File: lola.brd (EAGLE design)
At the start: 100 x 80 mm, 1 part, among them U1 ATMEGA328P_TQFP

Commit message: Base modules
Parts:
- added C1, C11, C14, C2, C3, C4, C7, C8, C9: 0.1uF, resistor:C0603
- added C10, C12, C13: 4.7uF, resistor:C0603
- added C5, C6: 22pF, resistor:C0603
- added CN1: (no value), adafruit:USB-MINIB
- added D1, D2: transil, SparkFun-DiscreteSemi:SOD-323
- added D3: (no value), SparkFun-DiscreteSemi:SMA-DIODE
- added F1, F3: 6V/0.5A, SparkFun-Fuses:1206
- added F2: (no value), adafruit:1812
- added IC1: FT232RL, ftdichip:SSOP28
- added IC2: MCP73833-UN, adafruit:MSOP10
- added L1: LQH32PN4R7NN0L, rcl:L1812
- added LED1, LED2: (no value), adafruit:CHIPLED_0805
- added Q1: (no value), SparkFun-DiscreteSemi:SOT23-3
- added R1, R5, R6, R9: 10K, resistor:R0603
- added R2: 1M, resistor:R0603
- added R3, R4: 1K, resistor:R0603
- added R7: 2K, resistor:R0603
- added R8: 10K ntc, resistor:R0603
- added U$1: MCP1603T-330I/OS, MCP1603T-330I_OS:SOT95P280X110-5N
- added U$2, U$3: COMF_BHC-18650-1P, FloManEagle:MR18650_HOLDER
- added U2: RFM69HW, SparkFun-RF:RFM69W-XXXS2
- added U3: AT24C256C-SSHL-T, AT24C256C-SSHL-T:SOIC127P600X175-8N
- added U4: ADS1115IDGST, ADS1115IDGST:SOP50P490X110-10N
- added X1: (no value), adafruit:SMA_EDGELAUNCH_UFL
- added Y1: 8MHz, SparkFun-Clocks:CRYSTAL-SMD-5X3.2-4PAD
- moved U1 59.9 mm to (10.7, 60.3), turned to 180 degrees
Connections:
- new net !EXT_RESET: C8.2, IC1.3
- new net !RESET: C8.1, R1.2, U1.29
- new net 3.3V: C1.1, C10.1, C11.1, C14.1, C2.1, C3.1, C4.1, C9.1, F3.2, R1.1, R5.2, R6.2, U1.18, U1.20, U1.4, U1.6, U2.8, U3.8, U4.8
- new net 5V: D3.A, F1.2, IC1.20, IC2.1, IC2.2, Q1.1, R9.2
- new net ADC_RDY: U4.2
- new net AIN0: U4.4
- new net AIN1: U4.5
- new net AIN2: U4.6
- new net AIN3: U4.7
- new net CHG: IC2.3
- new net FT_3.3V: C7.1, IC1.17, IC1.4, R3.2, R4.2
- new net FULL: IC2.4
- new net GND: C1.2, C10.2, C11.2, C12.2, C13.2, C14.2, C2.2, C3.2, C4.2, C5.2, C6.2, C7.2, C9.2, CN1.GND, D1.A, D2.A, IC1.18, IC1.21, IC1.25, IC1.7, IC2.5, R7.2, R8.2, R9.1, U$1.2, U$2.P$2, U$3.P$2, U1.21, U1.3, U1.5, U2.11, U2.9, U3.1, U3.2, U3.3, U3.4, U3.7, U4.1, U4.3, X1.GND@1, X1.GND@2, X1.GND@3, X1.GND@4, Y1.2, Y1.4
- new net MISO: U1.16, U2.13
- new net MOSI: U1.15, U2.14
- new net N$1: U2.10, X1.P
- new net N$10: U1.2
- new net N$11: U1.9
- new net N$12: U1.10
- new net N$13: U1.11
- new net N$14: U1.12
- new net N$15: U1.13
- new net N$16: U1.14
- new net N$17: C5.1, R2.2, U1.7, Y1.3
- new net N$18: C6.1, R2.1, U1.8, Y1.1
- new net N$19: IC2.8, R8.1
- new net N$2: F2.1, U$2.P$1
- new net N$20: CN1.VBUS, F1.1
- new net N$21: CN1.D+, D2.C, IC1.15
- new net N$22: CN1.D-, D1.C, IC1.16
- new net N$23: LED2.A, R4.1
- new net N$24: IC1.22, LED2.C
- new net N$25: IC1.23, LED1.C
- new net N$26: LED1.A, R3.1
- new net N$28: IC2.6, R7.1
- new net N$29: L1.2, U$1.5
- new net N$3: C13.1, F3.1, L1.1, U$1.4
- new net N$4: U1.23
- new net N$5: U1.24
- new net N$6: U1.25
- new net N$7: U1.26
- new net N$8: U1.32
- new net N$9: U1.1
- new net RF_INT: U2.2
- new net RF_SS: U2.15
- new net RX: IC1.1, U1.30
- new net SCK: U1.17, U2.12
- new net SCL: R5.1, U1.28, U3.6, U4.10
- new net SDA: R6.1, U1.27, U3.5, U4.9
- new net TX: IC1.5, U1.31
- new net VCC: D3.C, Q1.2, U$1.1, U$1.3
- new net V_BATT: C12.1, F2.2, IC2.10, IC2.9, Q1.3, U$3.P$1
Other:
- board size 100 x 80 mm -> 45 x 100 mm

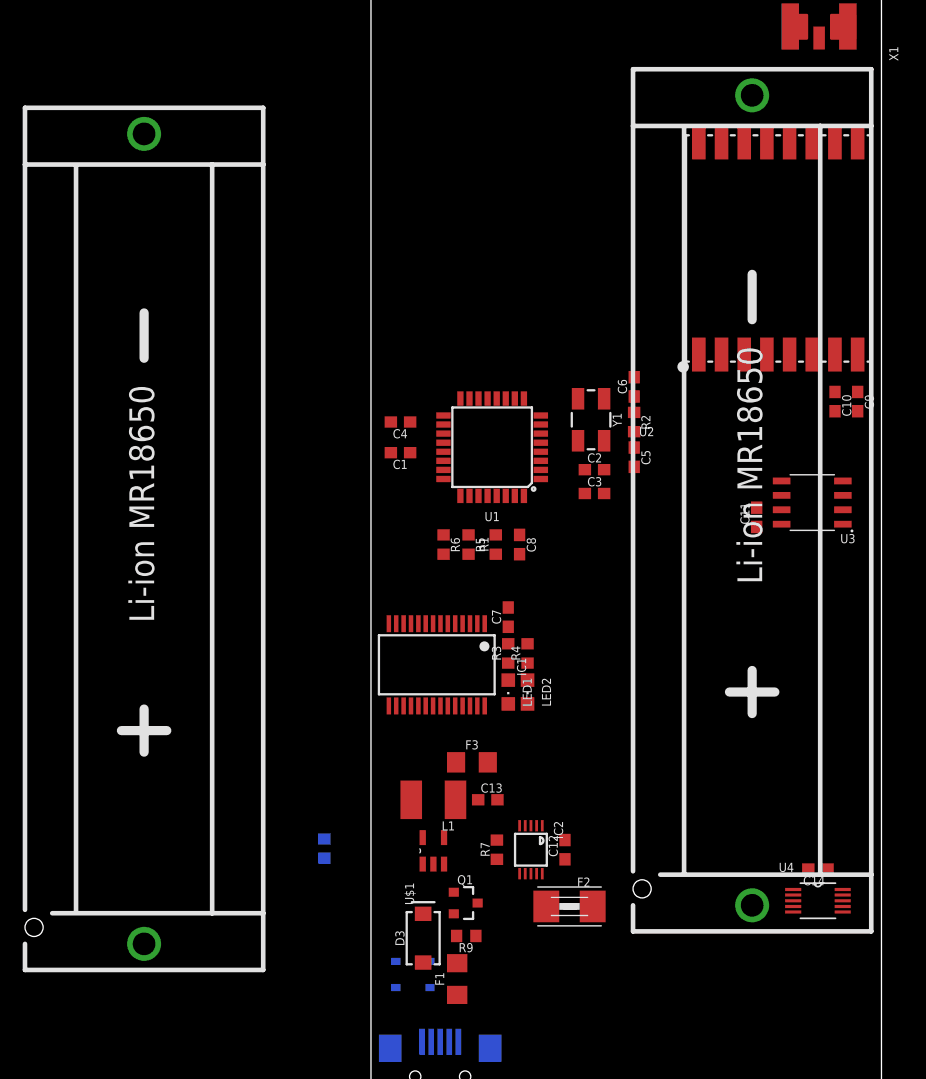
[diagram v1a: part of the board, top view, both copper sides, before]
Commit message: StepUp converter plus output-en
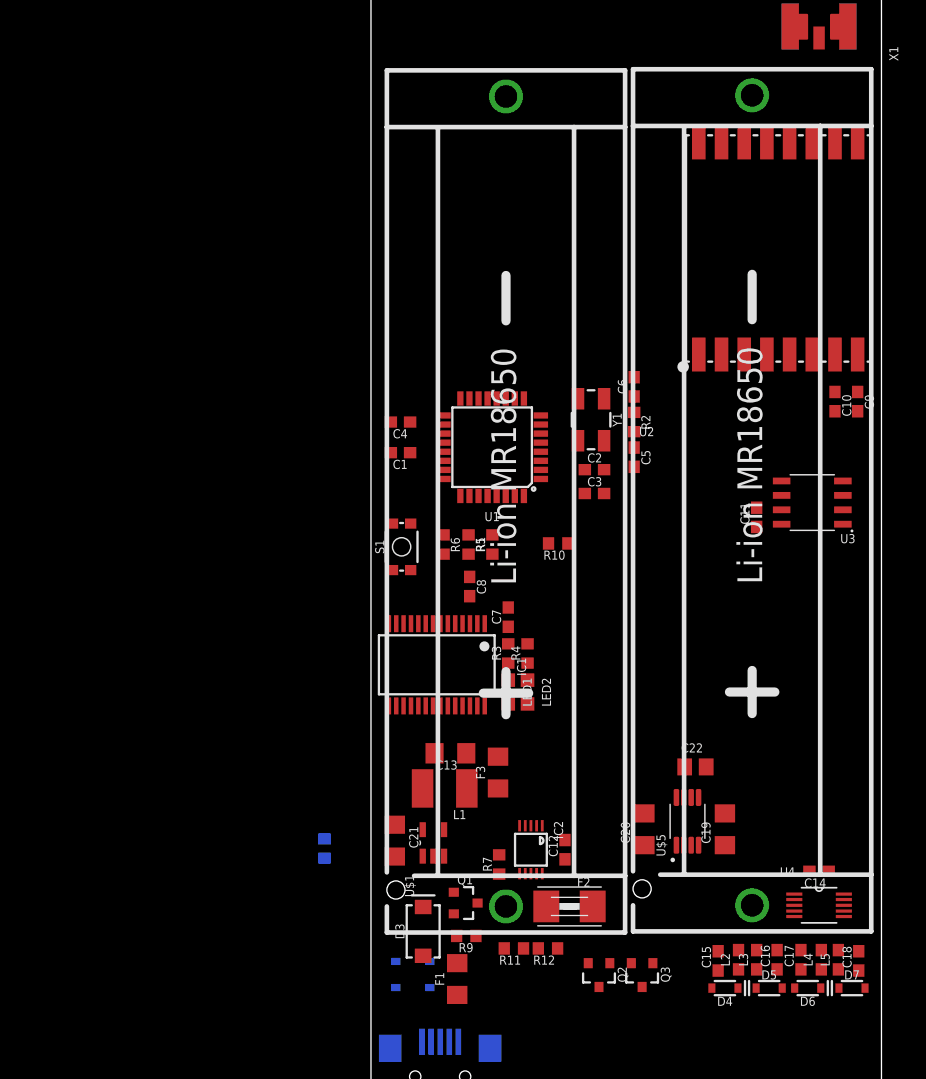
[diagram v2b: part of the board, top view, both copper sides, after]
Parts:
- added C15, C16, C17, C18: 10uF, resistor:C0603
- added C19, C20, C21: 10uF, resistor:C1206
- added C22: 1uF, resistor:C0805
- added D4, D5, D6, D7: transil, SparkFun-DiscreteSemi:SOD-323
- added L2, L3, L4, L5: ferrit, SparkFun-Coils:0603
- added Q2, Q3: DMG1013UWQ-7, SparkFun-DiscreteSemi:SOT23-3
- added R10: (no value), resistor:R0603
- added R11, R12: 100K, resistor:R0603
- added S1: (no value), SparkFun-Switches:TACTILE_SWITCH_SMD_4.6X2.8MM
- added U$5: MCP1252-33X50I/MS, MCP1252-33X50I_MS:SOP65P490X110-8N
- C13: device resistor:C0603 -> resistor:C1206
- moved U$3 32.1 mm to (11.9, 55.5)
- moved C8 5.75 mm to (8.70, 48.0)
- moved C13 5.26 mm to (7.00, 33.3), turned to 180 degrees
- moved F3 2.47 mm to (11.2, 31.6), turned to 90 degrees
- moved L1 1.41 mm to (6.50, 30.2)
- moved R7 1.32 mm to (11.3, 23.5)
- moved U$1 0.70 mm to (5.50, 25.4)
- moved D3 0.60 mm to (4.60, 17.6)
- moved U4 0.41 mm to (39.5, 19.9)
- moved R1 0.30 mm to (10.7, 51.7)
- moved C14 0.22 mm to (39.5, 22.9)
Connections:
- new net 5V_OUT: Q3.3
- new net A0: D4.C, L2.1
- new net A1: D5.C, L3.1
- new net A2: D6.C, L4.1
- new net A3: D7.C, L5.1
- new net BATT_SENSE: R11.1, R12.2
- new net BUCK_EN: U$5.7
- new net BUCK_PGD: U$5.1
- new net N$30: C20.1, Q3.2, U$5.2
- new net N$31: C22.1, U$5.6
- new net N$32: C22.2, U$5.5
- new net OUT_EN: Q2.1, Q3.1, R10.1
- new net PW_OUT: Q2.3
- net !RESET: now also S1.1, S1.2
- net 3.3V: now also Q2.2, R10.2
- net AIN0: now also C15.2, L2.2
- net AIN1: now also C16.2, L3.2
- net AIN2: now also C17.2, L4.2
- net AIN3: now also C18.2, L5.2
- net GND: now also C15.1, C16.1, C17.1, C18.1, C19.2, C20.2, C21.1, D4.A, D5.A, D6.A, D7.A, R12.1, S1.3, S1.4, U$5.4, U$5.8
- net VCC: now also C21.2
- net V_BATT: now also C19.1, R11.2, U$5.3

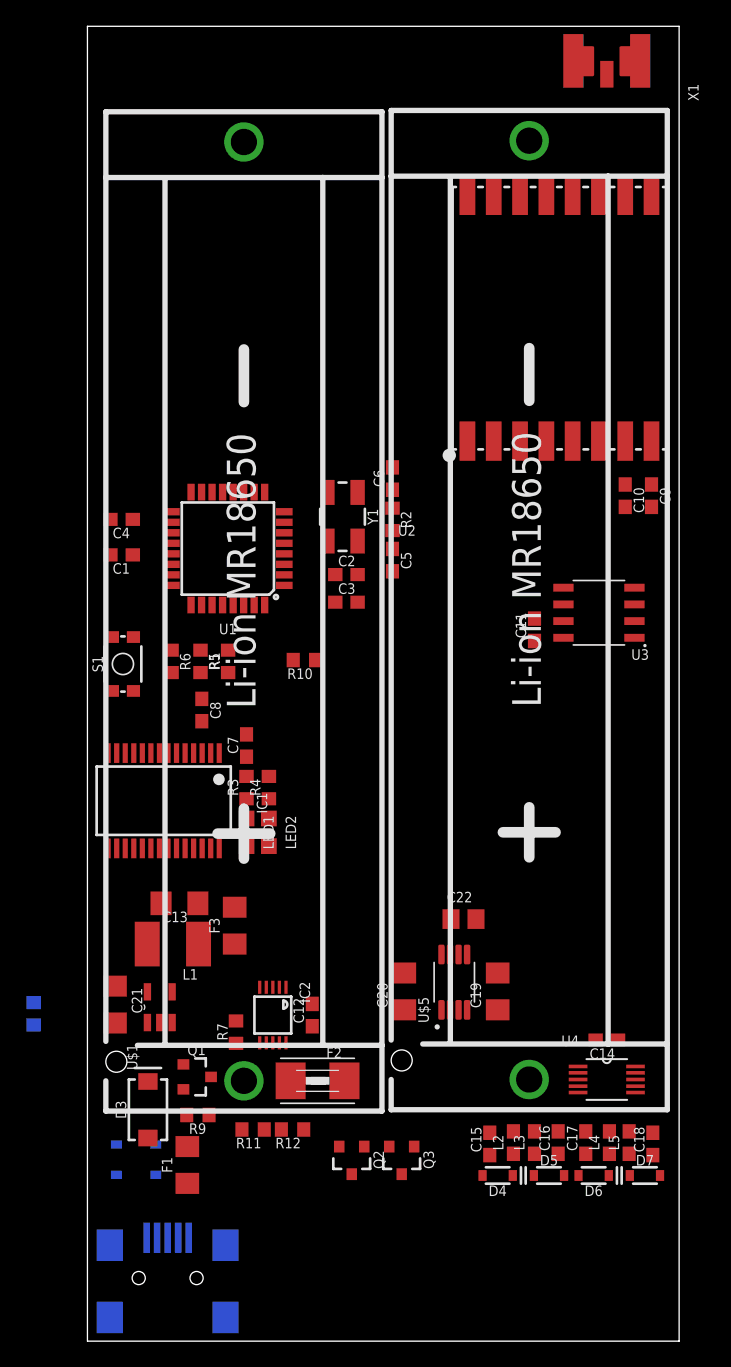
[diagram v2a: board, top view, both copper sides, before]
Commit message: rtc, step-up converter
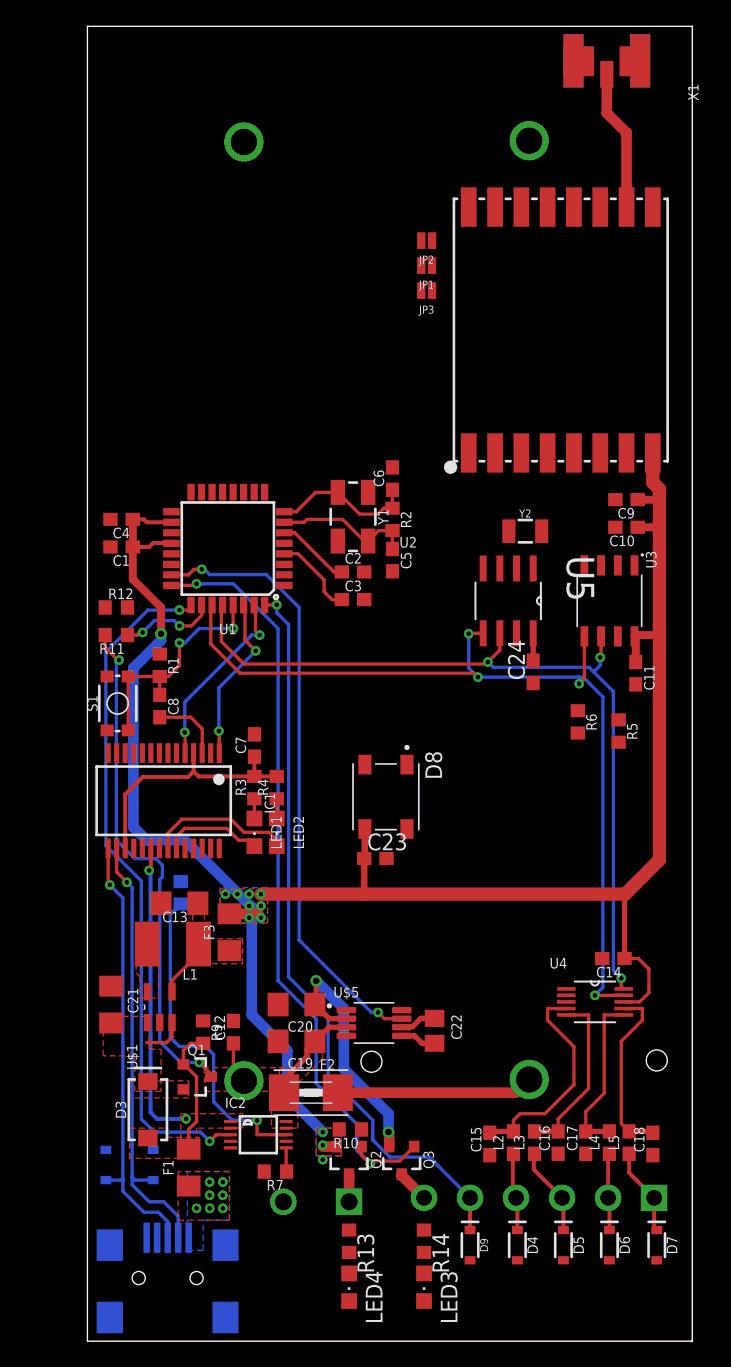
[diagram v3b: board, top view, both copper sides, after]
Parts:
- added C23: 1uF, resistor:C0603
- added C24: 0.1uF, resistor:C0603
- added D8: 1655, 1655:LED_1655
- added D9: transil, SparkFun-DiscreteSemi:SOD-323
- added J4: (no value), SparkFun-Connectors:SCREWTERMINAL-5MM-2
- added J7: (no value), SparkFun-Connectors:SCREWTERMINAL-3.5MM-6
- added JP1, JP2, JP3: (no value), SparkFun-Jumpers:SMT-JUMPER_2_NO_NO-SILK
- added LED3, LED4: (no value), adafruit:CHIPLED_0805
- added R13, R14: 2K, resistor:R0603
- added U5: DS1338Z-33+T&R, DS1338Z-33_T_R:SOIC127P600X175-8N
- added Y2: 32.768kHz, SparkFun-Clocks:CRYSTAL-SMD-3.2X1.5MM
- R10: value (none) -> 10K
- moved R12 41.9 mm to (2.20, 55.8), turned to 0 degrees
- moved R11 39.0 mm to (2.20, 53.7)
- moved R10 35.9 mm to (20.0, 16.1)
- moved R5 32.2 mm to (40.4, 46.4)
- moved R6 31.2 mm to (37.3, 47.1)
- moved C19 15.8 mm to (15.9, 22.8), turned to 180 degrees
- moved R8 14.5 mm to (7.10, 34.1)
- moved R7 11.0 mm to (14.3, 12.9), turned to 180 degrees
- moved IC2 9.17 mm to (13.0, 15.7), turned to 270 degrees
- moved C22 8.78 mm to (26.4, 23.6), turned to 270 degrees
- moved C11 8.38 mm to (41.7, 50.8), turned to 270 degrees
- moved C20 8.26 mm to (15.9, 25.6), turned to 180 degrees
- moved U$5 6.84 mm to (21.8, 24.2), turned to 0 degrees
- moved R9 6.31 mm to (8.80, 23.5), turned to 270 degrees
- moved C14 6.22 mm to (40.0, 29.1)
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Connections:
- removed net N$4: U1.23
- removed net N$9: U1.1
- new net NEO_LED: D8.2
- new net RMISO: JP1.1, U2.13
- new net RMOSI: JP2.1, U2.14
- new net RSCK: JP3.1, U2.12
- new net SDI: D9.C, J7.5, U1.32
- new net VBAT: U5.3
- net 3.3V: now also C23.1, C24.2, D8.3, U5.8
- net 5V_OUT: now also J7.6, R14.1
- net A0: now also J7.4
- net A1: now also J7.3
- net A2: now also J7.2
- net A3: now also J7.1
- net BATT_SENSE: now also U1.26
- net BUCK_EN: now also U1.23
- net CHG: now also U1.25
- net GND: now also C23.2, C24.1, D8.1, D9.A, J4.2, LED3.C, LED4.C, U5.4
- net MISO: now also JP1.2; no longer U2.13
- net MOSI: now also JP2.2; no longer U2.14
- net N$5: now also LED3.A, R14.2; no longer U1.24
- net N$6: now also U5.1, Y2.P$2; no longer U1.25
- net N$7: now also U5.2, Y2.P$1; no longer U1.26
- net N$8: now also LED4.A, R13.2; no longer U1.32
- net OUT_EN: now also U1.24
- net PW_OUT: now also J4.1, R13.1
- net RF_INT: now also U1.1
- net SCK: now also JP3.2; no longer U2.12
- net SCL: now also U5.6
- net SDA: now also U5.5
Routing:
- net 3.3V: track 0.00 -> 165.8 mm, vias 0 -> 12
- net SDA: track 0.00 -> 68.8 mm, vias 0 -> 4
- net SCL: track 0.00 -> 62.8 mm, vias 0 -> 3
- net OUT_EN: track 0.00 -> 58.6 mm, vias 0 -> 2
- net SDI: track 0.00 -> 56.3 mm, vias 0 -> 1
- net CHG: track 0.00 -> 52.5 mm, vias 0 -> 2
- net V_BATT: track 0.00 -> 50.4 mm, vias 0 -> 2
- net BUCK_EN: track 0.00 -> 46.7 mm, vias 0 -> 2
- net N$22: track 0.00 -> 33.9 mm, vias 0 -> 1
- net N$21: track 0.00 -> 33.5 mm, vias 0 -> 1
- net 5V: track 0.00 -> 33.0 mm, vias 0 -> 2
- net N$19: track 0.00 -> 25.1 mm, vias 0 -> 1
- net N$30: track 0.00 -> 19.6 mm, vias 0 -> 2
- net FT_3.3V: track 0.00 -> 19.4 mm
- net !RESET: track 0.00 -> 17.8 mm, vias 0 -> 2
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- added copper zone on layer 1, net 3.3V
- added copper zone on layer 16, net 3.3V
- added copper zone on layer 1, net 5V
- added copper zone on layer 1, net N$20
- added copper zone on layer 16, net N$20
- added copper zone on layer 1, net N$29
- added copper zone on layer 1, net N$3
- added copper zone on layer 1, net VCC
- added copper zone on layer 1, net V_BATT
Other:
- board size 45 x 100 mm -> 46 x 100 mm

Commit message: Feliratozás van hátra + kondi + buzzer
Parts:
- added C25, C26: 0.1uF, resistor:C0603
- added J1: (no value), SparkFun-Connectors:1X04_LOCK_LONGPADS
- added J3: (no value), SparkFun-Connectors:1X06_NO_SILK
- added S2: (no value), SparkFun-Switches:TACTILE_SWITCH_SMD_4.6X2.8MM
- added U$4: OLED_0.96_I2C, tft_1.8_1.44_oled_0.96:OLED_0.96_I2C
- added U$6: (no value), FloManEagle:LOLA_LOGO_LAYER
- added U$7: (no value), FloManEagle:MRFLOW
- added U6: SHT21, SHT21:SON100P300X300X110-7N
- moved LED3 10.5 mm to (15.4, 6.50), turned to 90 degrees
- moved LED4 6.16 mm to (15.4, 8.30), turned to 90 degrees
- moved JP3 5.70 mm to (25.7, 74.2)
- moved JP1 5.40 mm to (25.7, 76.4)
- moved JP2 5.00 mm to (25.7, 78.7)
- moved R5 1.64 mm to (39.4, 47.7)
- moved R14 1.14 mm to (24.7, 8.30), turned to 180 degrees
- moved R13 1.06 mm to (19.1, 8.30), turned to 180 degrees
- moved R11 0.94 mm to (2.70, 52.9), turned to 270 degrees
- moved R6 0.60 mm to (37.3, 47.7)
- moved C3 0.40 mm to (20.2, 56.8)
- moved CN1 0.30 mm to (6.10, 4.10)
- moved C11 0.20 mm to (41.5, 50.8)
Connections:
- removed net N$10: U1.2
- removed net N$11: U1.9
- removed net N$12: U1.10
- removed net N$16: U1.14
- new net EXP: U6.7
- new net SW: S2.1, S2.2, U1.14
- net !RESET: now also J3.3
- net 3.3V: now also C25.1, C26.2, J1.2, J3.1, U$4.VCC, U6.5
- net ADC_RDY: now also U1.9
- net GND: now also C25.2, C26.1, J1.1, J3.2, S2.3, S2.4, U$4.GND, U6.2
- net MISO: now also J3.5
- net MOSI: now also J3.6
- net NEO_LED: now also U1.2
- net RF_SS: now also U1.10
- net SCK: now also J3.4
- net SCL: now also J1.4, U$4.SCL, U6.6
- net SDA: now also J1.3, U$4.SDA, U6.1
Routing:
- net 3.3V: track 165.8 -> 277.5 mm, vias 12 -> 15
- net SCL: track 62.8 -> 127.6 mm, vias 3 -> 5
- net ADC_RDY: track 0.00 -> 57.2 mm, vias 0 -> 2
- net SDA: track 68.8 -> 117.1 mm, vias 4 -> 5
- net MOSI: track 0.00 -> 41.6 mm, vias 0 -> 1
- net MISO: track 0.00 -> 37.9 mm, vias 0 -> 1
- net SCK: track 0.00 -> 35.3 mm, vias 0 -> 1
- net RF_SS: track 0.00 -> 34.5 mm, vias 0 -> 2
- net RF_INT: track 0.00 -> 27.5 mm
- net !RESET: track 17.8 -> 42.8 mm, vias 2 -> 3
- net SW: track 0.00 -> 22.8 mm
- net NEO_LED: track 0.00 -> 19.1 mm, vias 0 -> 2
- net RSCK: track 0.00 -> 17.8 mm
- net RMISO: track 0.00 -> 15.3 mm
- net RMOSI: track 0.00 -> 12.9 mm
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- added copper zone on layer 1, net GND
- added copper zone on layer 16, net GND
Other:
- outline, holes or cut-outs redrawn
- board text added: "2020.05.17."
- board text added: "Rev. 4."

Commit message: v1
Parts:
- added C27: 100uF, resistor:CT6032
- added LED5: (no value), adafruit:CHIPLED_0805
- added R15: 10K, resistor:R0603
- added T1, T2: (no value), transistor:SC59-BEC
- added U$10, U$15: (no value), FloManEagle:MINUS_LOGO
- added U$11: (no value), FloManEagle:ESD_LOGO
- added U$12: (no value), FloManEagle:TONNE_LOGO
- added U$13: (no value), FloManEagle:AGRO_SMALL_LOGO
- added U$14: (no value), FloManEagle:SOUND_ICON
- added U$16, U$17: (no value), FloManEagle:PLUS_LOGO
- added U$18, U$19: (no value), FloManEagle:BATTERY_LOGO
- added U$20: (no value), FloManEagle:CE_LOGO
- added U$8: BUZZER_5X9.6, FloManEagle:BUZZER_5X9.6
- added U$9: (no value), FloManEagle:RADIO_LOGO
- moved U$7 16.3 mm to (14.3, 44.5)
- moved C23 3.53 mm to (18.7, 38.2), turned to 90 degrees
- moved D8 2.30 mm to (22.7, 39.1)
- moved F2 0.40 mm to (17.0, 19.3)
- moved S1 0.30 mm to (2.30, 48.8)
- moved R11 0.20 mm to (2.70, 53.1)
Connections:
- removed net N$14: U1.12
- removed net N$15: U1.13
- new net BUZZER: T1.B, U1.12
- new net LED: T2.B, U1.13
- new net N$11: T1.C, U$8.-
- new net N$4: LED5.A, R15.1
- new net N$9: LED5.C, T2.C
- net 3.3V: now also R15.2, U$8.+
- net 5V: now also C27.-
- net GND: now also C27.+, T1.E, T2.E
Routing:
- net 3.3V: track 277.5 -> 297.4 mm
- net LED: track 0.00 -> 19.1 mm
- net GND: track 0.00 -> 11.2 mm, vias 0 -> 120
- net BUZZER: track 0.00 -> 9.06 mm
- net N$9: track 0.00 -> 6.58 mm, vias 1 -> 0
- net N$11: track 0.00 -> 6.10 mm
- net NEO_LED: track 19.1 -> 21.0 mm
- net N$4: track 0.00 -> 1.60 mm, vias 1 -> 0
- net FT_3.3V: track 19.4 -> 18.9 mm
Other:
- board text added: "1"
- board text added: "2"
- board text added: "3.3V"
- board text added: "5V"
- board text added: "A0"
- board text added: "A1"
- board text added: "A2"
- board text added: "A3"
- board text added: "Bypass"
- board text added: "Florian Szekely Agro Services & Solutions Kft."
- board text added: "GND"
- board text added: "MISO"
- board text added: "MOSI"
- board text added: "Node Module - 868MHz - Li-ion (Single Cell) Arduino Compatible (Lillypad) Analog/SDI/I2C/SPI"
- board text added: "Reset"
- board text added: "SCK"
- board text added: "SCL"
- board text added: "SDA"
- board text added: "SDI"

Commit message: Ordered version
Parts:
- moved U$13 1.30 mm to (19.9, 27.6)
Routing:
- net OUT_EN: track 58.4 -> 59.7 mm
- net GND: track 11.2 -> 12.5 mm
- net N$3: track 2.65 -> 3.22 mm
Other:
- outline, holes or cut-outs redrawn
